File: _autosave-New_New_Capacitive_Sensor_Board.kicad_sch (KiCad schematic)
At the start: 19 parts, among them IC1 FDC2212QDNTTQ1, J1 Conn_01x04_Pin, J2 Conn_01x04_Pin, J3 Conn_01x02_Pin, J4 Conn_01x02_Pin

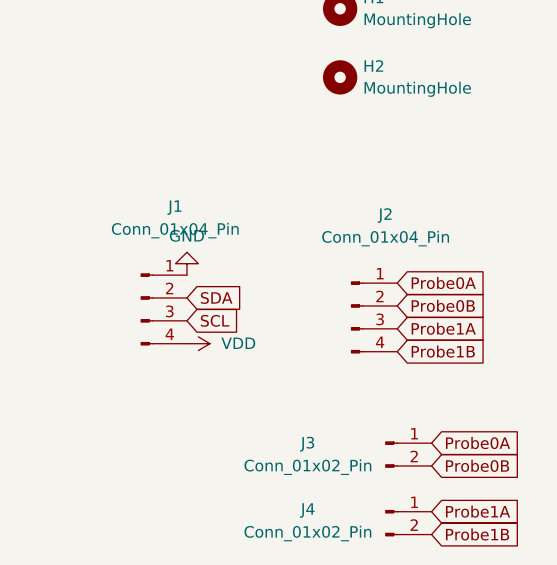
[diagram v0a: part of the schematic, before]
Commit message: Changed to nanofits and ordering stuff
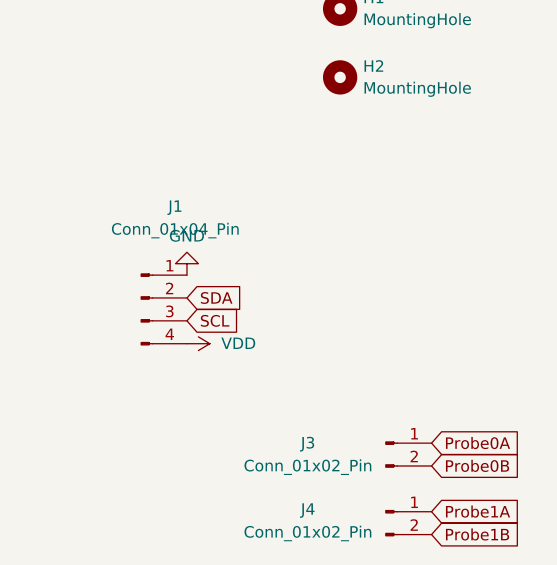
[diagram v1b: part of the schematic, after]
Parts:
- removed J2: Conn_01x04_Pin, Connector_Molex:Molex_Nano-Fit_105313-xx04_1x04_P2.50mm_Horizontal, symbol Connector:Conn_01x04_Pin
